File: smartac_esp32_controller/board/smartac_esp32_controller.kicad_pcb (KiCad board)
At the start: 2 copper layers, 60 x 60 mm, 19 parts, among them J1 Conn_01x03_Pin, M1 MountingHole_3.2mm_M3, M2 MountingHole_3.2mm_M3, M3 MountingHole_3.2mm_M3, M4 MountingHole_3.2mm_M3, Q1 2N2222A, U1 ESP32-DevKitC

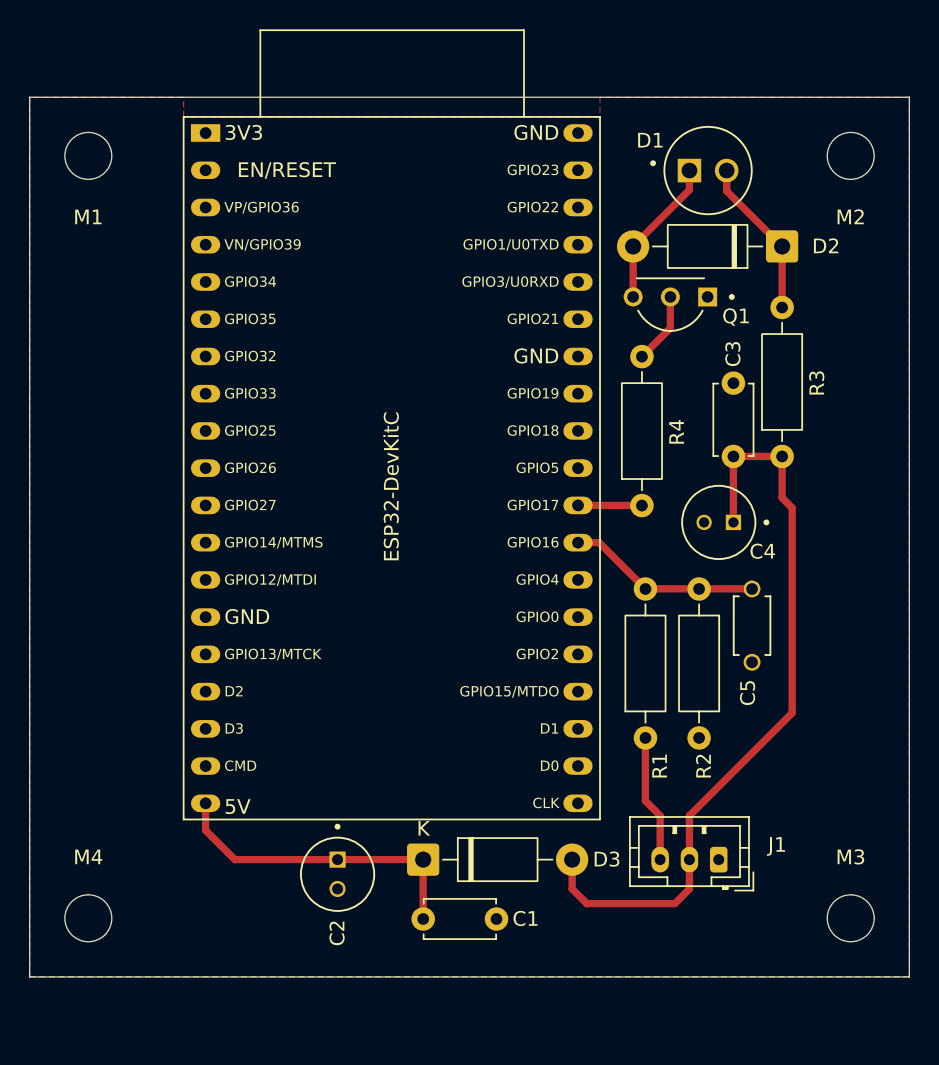
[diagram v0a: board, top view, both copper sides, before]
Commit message: Remaping GPIOs: 16 -> 4, 17 -> 5
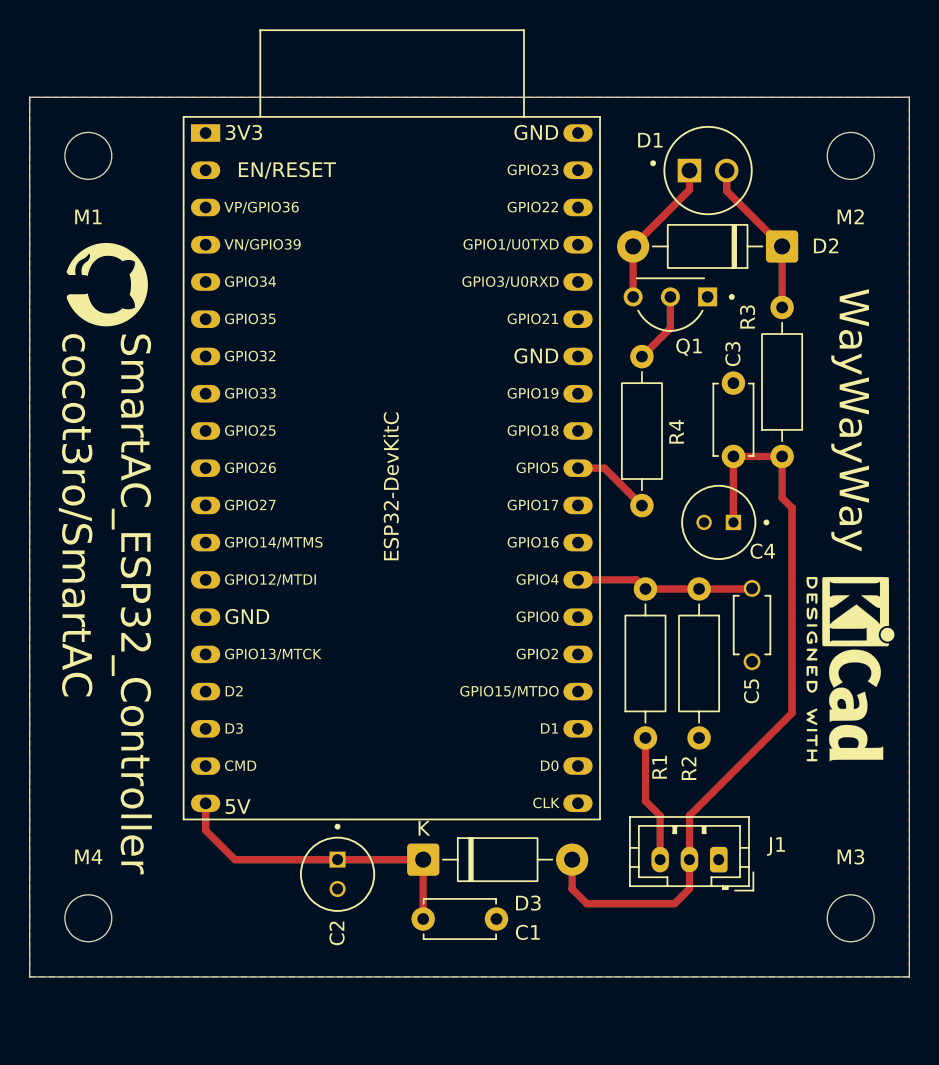
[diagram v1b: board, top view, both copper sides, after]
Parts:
- added G***: LOGO, Images:GitHub-logo-7x7, F.Cu at (37.0, -43.0)
- added REF**: KiCad-Logo2_5mm_SilkScreen, Symbol:KiCad-Logo2_5mm_SilkScreen, F.Cu at (88.0, -17.0)
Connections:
- C5 pad 2: /GPIO_16 -> /GPIO_4
- R1 pad 2: /GPIO_16 -> /GPIO_4
- R2 pad 1: /GPIO_16 -> /GPIO_4
- R4 pad 1: /GPIO_17 -> /GPIO_5
- U1 pad 26: unconnected-(U1-ADC2_CH0/GPIO4-Pad26) -> /GPIO_4
- U1 pad 27: /GPIO_16 -> unconnected-(U1-GPIO16-Pad27)
- U1 pad 28: /GPIO_17 -> unconnected-(U1-GPIO17-Pad28)
- U1 pad 29: unconnected-(U1-GPIO5-Pad29) -> /GPIO_5
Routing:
- net /GPIO_16: track 13.2 -> 0.00 mm
- net /GPIO_4: track 0.00 -> 12.1 mm
- net /GPIO_5: track 0.00 -> 5.42 mm
- net /GPIO_17: track 4.36 -> 0.00 mm
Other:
- board text added: "SmartAC_ESP32_Controller"
- board text added: "WayWayWay"
- board text added: "cocot3ro/SmartAC"

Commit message: SmartAC board
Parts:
- removed REF**: KiCad-Logo2_5mm_SilkScreen, Symbol:KiCad-Logo2_5mm_SilkScreen
- moved C1 12.9 mm to (51.0, 1.00), turned to 90 degrees
- moved C2 7.00 mm to (46.0, -3.00)
- moved D3 3.54 mm to (55.9, -2.00)
- moved G*** 3.00 mm to (37.0, -40.0)
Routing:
- net Net-(D3-K): track 21.6 -> 15.5 mm
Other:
- board text removed: "WayWayWay"
